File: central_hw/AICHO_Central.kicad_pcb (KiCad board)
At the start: 2 copper layers, 0 parts

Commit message: central_hw: Layout & routing
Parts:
- added C10: 100n, Capacitor_SMD:C_0402_1005Metric, F.Cu at (110.8, 125.0)
- added C11: 10u 50V, Capacitor_SMD:C_0805_2012Metric, F.Cu at (205.1, 118.2)
- added C12: 10u 50V, Capacitor_SMD:C_0805_2012Metric, F.Cu at (203.1, 118.2)
- added C13: 100n, Capacitor_SMD:C_0402_1005Metric, F.Cu at (201.6, 118.8)
- added C14: 100n, Capacitor_SMD:C_0402_1005Metric, F.Cu at (197.2, 117.2)
- added C15: 22u 25V, Capacitor_SMD:C_0805_2012Metric, F.Cu at (196.0, 119.1)
- added C16: 22u 25V, Capacitor_SMD:C_0805_2012Metric, F.Cu at (196.0, 121.1)
- added C17: 75p, Capacitor_SMD:C_0402_1005Metric, F.Cu at (200.1, 115.2)
- added C18: 470u 10V, Capacitor_SMD:CP_Elec_6.3x7.7, F.Cu at (190.0, 119.5)
- added C21: 100u 50V, Capacitor_SMD:CP_Elec_6.3x7.7, F.Cu at (125.0, 105.0)
- added C22: 100u 50V, Capacitor_SMD:CP_Elec_6.3x7.7, F.Cu at (155.5, 105.0)
- added C23: 100u 50V, Capacitor_SMD:CP_Elec_6.3x7.7, F.Cu at (185.5, 105.0)
- added C24: 100u 50V, Capacitor_SMD:CP_Elec_6.3x7.7, F.Cu at (215.5, 105.0)
- added H1: MountingHole, MountingHole:MountingHole_2.2mm_M2_Pad_Via, F.Cu at (102.5, 127.5)
- added H2: MountingHole, MountingHole:MountingHole_2.2mm_M2_Pad_Via, F.Cu at (217.5, 127.5)
- added H3: MountingHole, MountingHole:MountingHole_2.2mm_M2_Pad_Via, F.Cu at (217.5, 112.5)
- added H4: MountingHole, MountingHole:MountingHole_2.2mm_M2_Pad_Via, F.Cu at (122.0, 112.5)
- added J1: DC D5.5, Connector_BarrelJack:BarrelJack_Kycon_KLDX-0202-xC_Horizontal, F.Cu at (114.2, 117.5)
- added J2: P2.54 2x20, Connector_PinHeader_2.54mm:PinHeader_2x20_P2.54mm_Vertical, F.Cu at (184.1, 125.7)
- added J21: PH2.0, Connector_JST:JST_PH_S3B-PH-SM4-TB_1x03-1MP_P2.00mm_Horizontal, F.Cu at (115.5, 105.0)
- added J22: PH2.0, Connector_JST:JST_PH_S3B-PH-SM4-TB_1x03-1MP_P2.00mm_Horizontal, F.Cu at (145.5, 105.0)
- added J23: PH2.0, Connector_JST:JST_PH_S3B-PH-SM4-TB_1x03-1MP_P2.00mm_Horizontal, F.Cu at (175.5, 105.0)
- added J24: PH2.0, Connector_JST:JST_PH_S3B-PH-SM4-TB_1x03-1MP_P2.00mm_Horizontal, F.Cu at (205.5, 105.0)
- added J3: P2.54 1x03, Connector_PinSocket_2.54mm:PinSocket_1x03_P2.54mm_Vertical, F.Cu at (190.5, 128.3)
- added J31: PH2.0, Connector_JST:JST_PH_S2B-PH-SM4-TB_1x02-1MP_P2.00mm_Horizontal, F.Cu at (105.0, 105.0)
- added J32: PH2.0, Connector_JST:JST_PH_S2B-PH-SM4-TB_1x02-1MP_P2.00mm_Horizontal, F.Cu at (135.0, 105.0)
- added J33: PH2.0, Connector_JST:JST_PH_S2B-PH-SM4-TB_1x02-1MP_P2.00mm_Horizontal, F.Cu at (165.0, 105.0)
- added J34: PH2.0, Connector_JST:JST_PH_S2B-PH-SM4-TB_1x02-1MP_P2.00mm_Horizontal, F.Cu at (195.0, 105.0)
- added L1: 10u, Inductor_SMD:L_Sunlord_SWPA4030S, F.Cu at (200.5, 123.0)
- added R10: 4.7, Resistor_SMD:R_0402_1005Metric, F.Cu at (111.8, 125.0)
- added R11: 200k, Resistor_SMD:R_0402_1005Metric, F.Cu at (199.2, 115.2)
- added R12: 27k, Resistor_SMD:R_0402_1005Metric, F.Cu at (197.8, 115.7)
- added R31: 100k, Resistor_SMD:R_0402_1005Metric, F.Cu at (106.6, 110.6)
- added R32: 100k, Resistor_SMD:R_0402_1005Metric, F.Cu at (136.6, 110.6)
- added R33: 100k, Resistor_SMD:R_0402_1005Metric, F.Cu at (166.6, 110.6)
- added R34: 100k, Resistor_SMD:R_0402_1005Metric, F.Cu at (196.6, 110.6)
- added U1: TPS54302, Package_TO_SOT_SMD:SOT-23-6, F.Cu at (199.4, 118.2)
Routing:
- net +24V: track 0.00 -> 146.6 mm
- net +3.3V: track 0.00 -> 112.8 mm, vias 0 -> 6
- net /UART_3: track 0.00 -> 70.5 mm
- net /UART_4: track 0.00 -> 51.2 mm
- net /BTN_A: track 0.00 -> 50.3 mm
- net /UART_2: track 0.00 -> 36.3 mm
- net +5V: track 0.00 -> 31.8 mm
- net /BTN_B: track 0.00 -> 29.0 mm
- net /BTN_D: track 0.00 -> 26.4 mm
- net /UART_0_RX: track 0.00 -> 22.8 mm
- net /UART_5: track 0.00 -> 21.3 mm
- net /BTN_C: track 0.00 -> 19.9 mm
- net /UART_0_TX: track 0.00 -> 17.5 mm
- net Net-(U1-SW): track 0.00 -> 10.6 mm, vias 0 -> 2
- net GND: track 0.00 -> 3.83 mm, vias 0 -> 159
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- added copper zone on B.Cu, net GND
- added copper zone on F.Cu, net GND
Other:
- board outline added: 120 x 30 mm

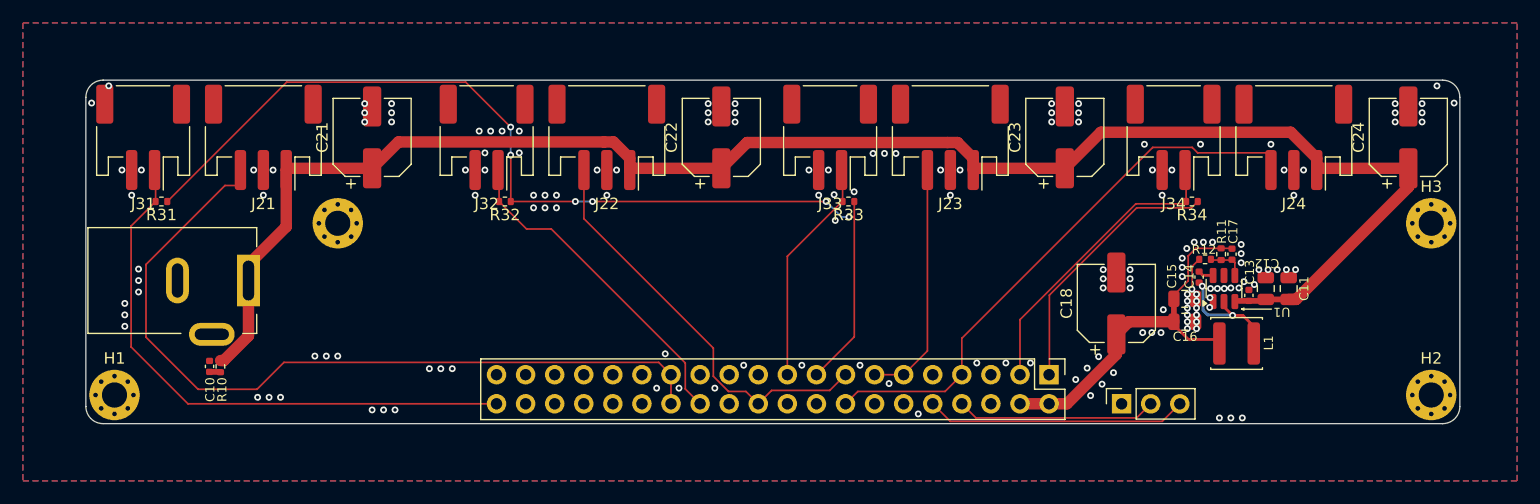
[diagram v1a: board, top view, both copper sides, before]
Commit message: central_hw: Edit silkscreen & finalize
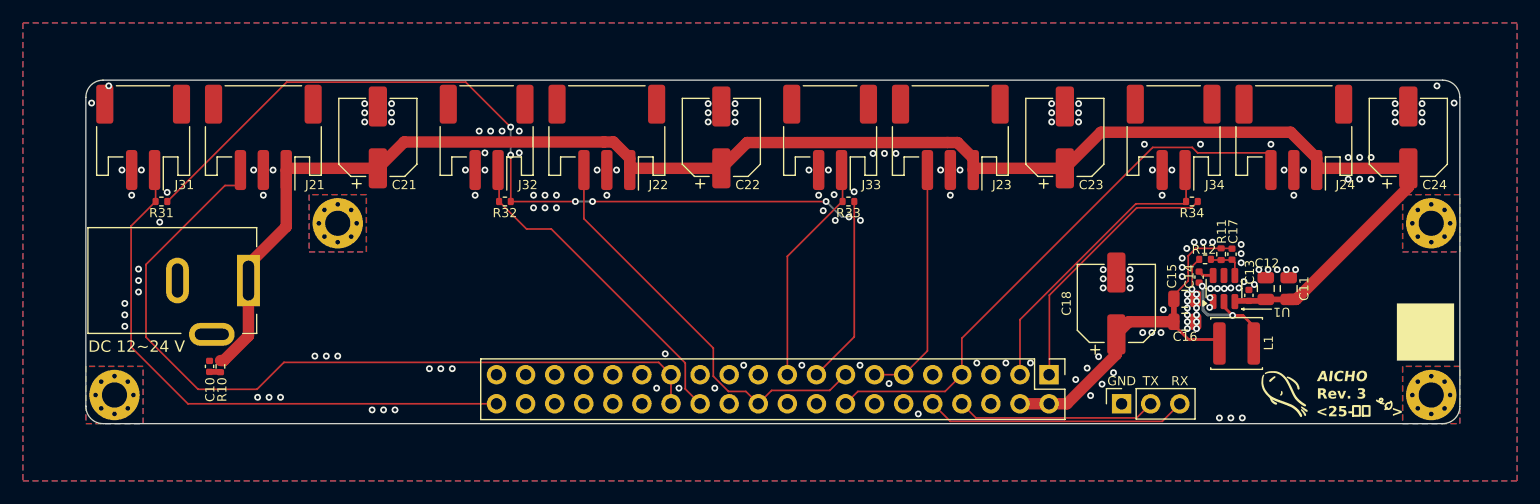
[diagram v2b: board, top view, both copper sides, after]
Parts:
- added G***: LOGO, LOGO, F.Cu at (204.8, 127.5)
- moved C21 0.50 mm to (125.5, 105.0)
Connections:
- H1 pad 1: (no net) -> GND
- H2 pad 1: (no net) -> GND
- H3 pad 1: (no net) -> GND
- H4 pad 1: (no net) -> GND
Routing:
- net GND: vias 159 -> 169
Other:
- board text added: "<25-"
- board text added: ">"
- board text added: "AICHO"
- board text added: "DC 12~24 V"
- board text added: "GND"
- board text added: "RX"
- board text added: "Rev. 3"
- board text added: "TX"
- board text added: "ayu.land/aicho?id=R3_Cxx"
- board text added: "寒露"
